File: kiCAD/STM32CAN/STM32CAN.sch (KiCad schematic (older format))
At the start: 25 parts, among them IC1 TPS560430X3FDBVR, J1 Conn_02x12_Odd_Even, J2 DB9_Male, J3 Conn_02x05_Odd_Even, U1 STM32F042F6Px, U2 TCAN332, Y1 Crystal

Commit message: Updated kiCAD drawing
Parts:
- removed D1: D_Schottky, symbol Device:D_Schottky
- removed IC1: TPS560430X3FDBVR, SOT95P280X145-6N, symbol SamacSys_Parts:TPS560430X3FDBVR
- removed L1: 6.8uH, symbol pspice:INDUCTOR
- removed R2: 51k, symbol Device:R
- removed R3: 22.1k, symbol Device:R
- added D1: PMEG6010CEJ, Diode_SMD:D_SOD-323, symbol Diode:PMEG6010CEJ
- added IC1: LMZM23601V3, SamacSys_Parts:LMZM23601V5SILR, symbol SamacSys_Parts:LMZM23601V3
- C1, C2, C3, C4, C5, C6, C7: footprint (none) -> Capacitor_SMD:C_0603_1608Metric
- C10: value 0.1uF -> 47uF; footprint (none) -> Capacitor_SMD:C_1206_3216Metric; Field4 (none) -> C3216X5R1E476M160AC
- C11: value 10uF -> 1uF; footprint (none) -> Capacitor_SMD:C_0603_1608Metric
- C8: value C -> 100nF; footprint (none) -> Capacitor_SMD:C_0603_1608Metric
- C9: value 2.2uF -> 10uF; footprint (none) -> Capacitor_SMD:C_0805_2012Metric; Field4 (none) -> C2012X5R1V106K085AC
- D2: footprint (none) -> Diode_SMD:D_0603_1608Metric
- J1: footprint (none) -> Connector_PinHeader_1.27mm:PinHeader_2x12_P1.27mm_Vertical_SMD
- J2: footprint (none) -> Connector_Dsub:DSUB-9_Male_Horizontal_P2.77x2.54mm_EdgePinOffset9.40mm
- J3: footprint (none) -> Connector_PinHeader_1.27mm:PinHeader_2x05_P1.27mm_Vertical_SMD
- R1: value R -> 470R; footprint (none) -> Resistor_SMD:R_0603_1608Metric
- R4: footprint (none) -> Resistor_SMD:R_0603_1608Metric
- U2: footprint (none) -> Package_SO:SOIC-8_3.9x4.9mm_P1.27mm
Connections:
- net GNDPWR is gone; now on net GNDREF: C11.2, C9.2, J2.6
- net +3V3: now also C10.1, IC1.6 (VOUT), IC1.7 (FB)
- net GNDREF: now also C10.2, IC1.1 (GND), IC1.11 (EP), IC1.2 (MODE/SYNC)
- net POWER_IN: now also D1.2 (A)
- net at C9.1: now also D1.1 (K), IC1.3 (VIN), IC1.4 (EN)
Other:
- moved on the sheet: C8

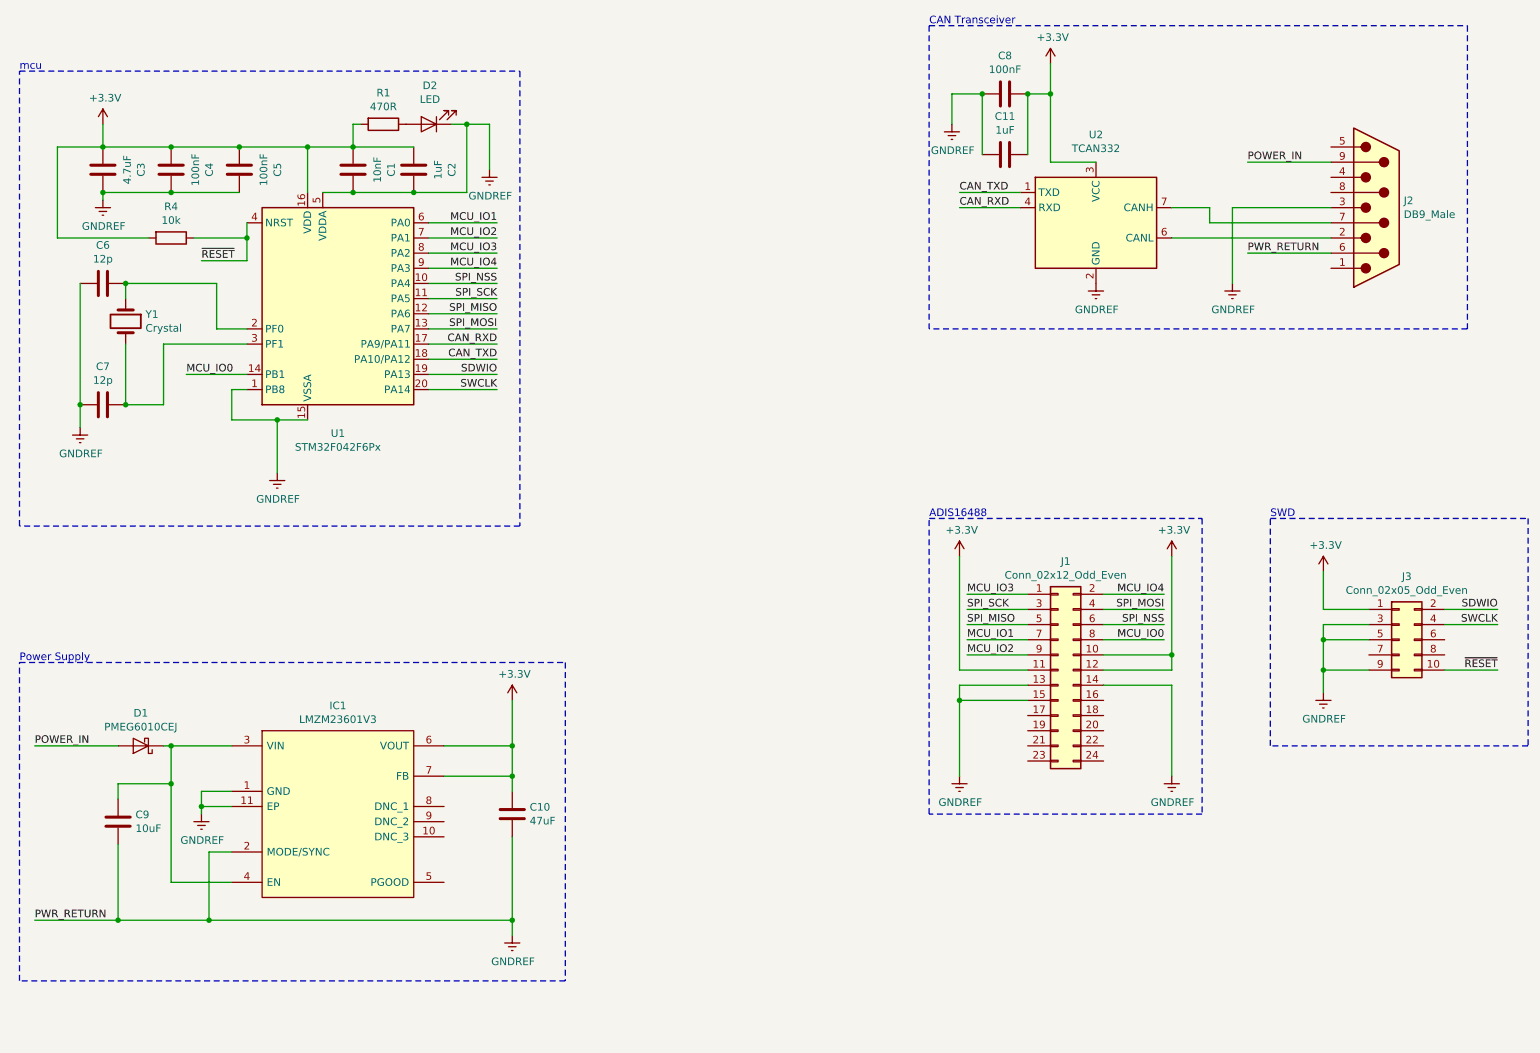
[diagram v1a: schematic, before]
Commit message: Started layout
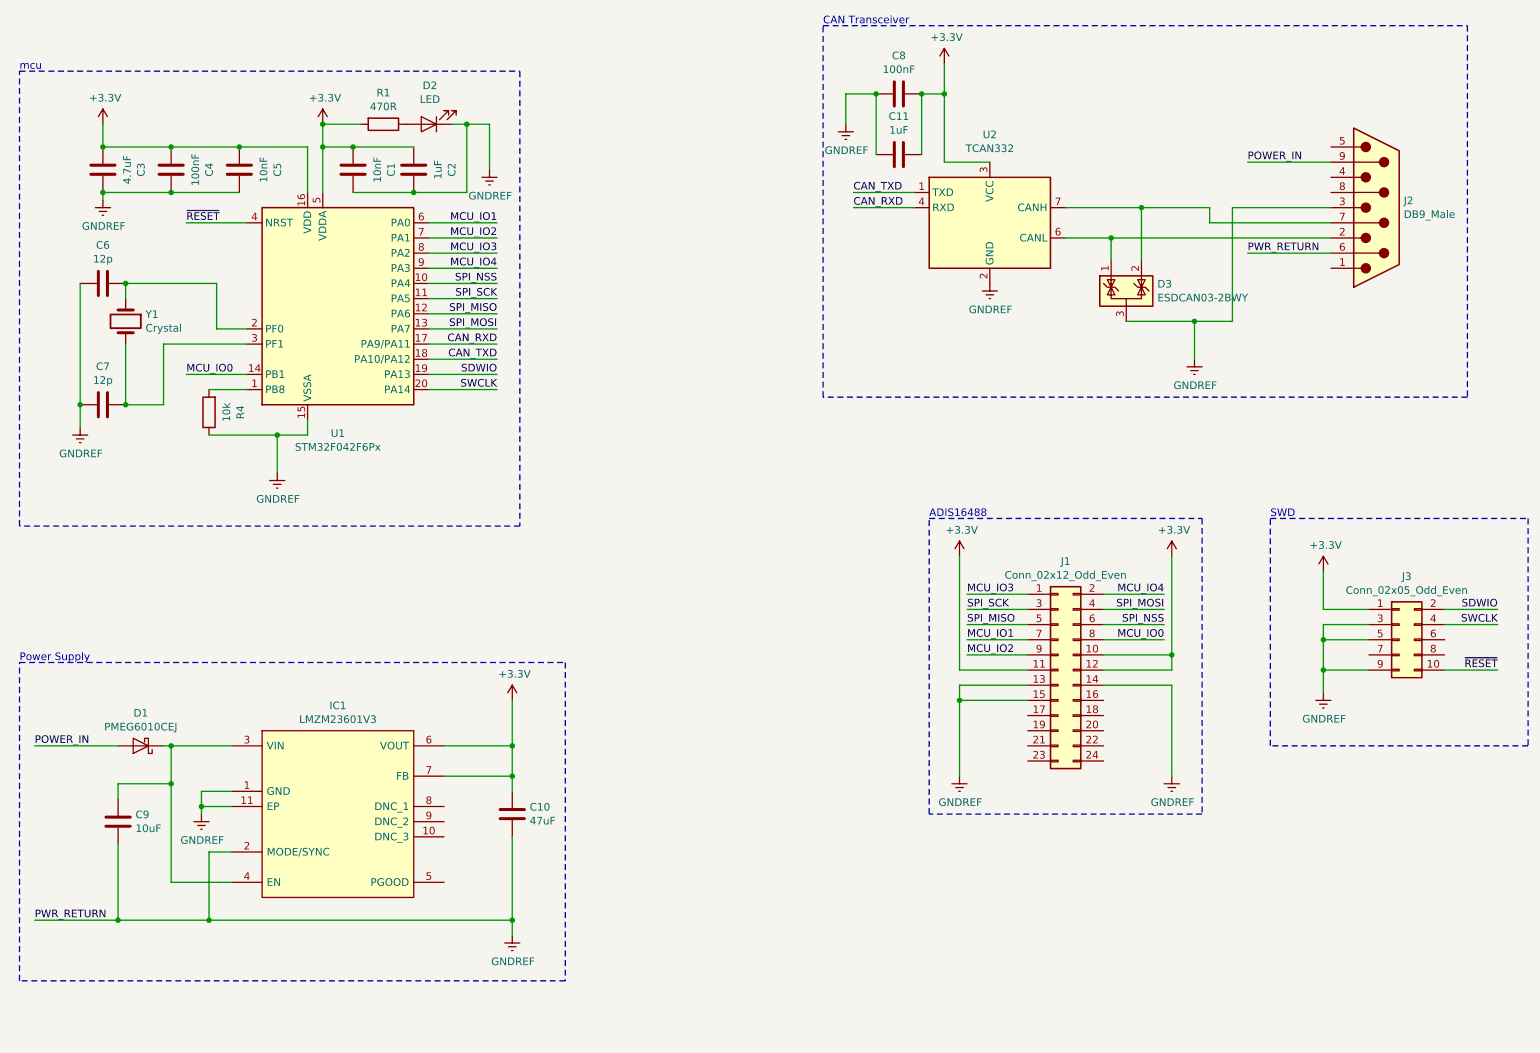
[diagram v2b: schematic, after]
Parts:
- added D3: ESDCAN03-2BWY, Package_TO_SOT_SMD:SOT-323_SC-70, symbol Power_Protection:NUP2105L
- C5: value 100nF -> 10nF
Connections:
- net +3V3: now also U1.5 (VDDA); no longer R4.2
- net GNDREF: now also R4.1, D3.3 (A); no longer U1.1 (PB8), U1.5 (VDDA)
- net ~RESET: no longer R4.1
- net at J2.2, U2.6 (CANL): now also D3.1 (K)
- net at J2.7, U2.7 (CANH): now also D3.2 (K)
- new net: R4.2, U1.1 (PB8)
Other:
- moved on the sheet: C11, C8, U2
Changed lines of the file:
@@
 	1    0    0    -1
 $EndComp
-Wire Wire Line
-	2500 3200 2400 3200
 $Comp
 L power:GNDREF #PWR0103
@@
 Text Label 4150 3200 2    50   ~ 0
 SWCLK
-Text Label 2200 2350 0    50   ~ 0
+Text Label 2100 2100 0    50   ~ 0
 ~RESET
 Text Label 4150 2500 2    50   ~ 0
@@
 	1    0    0    -1
 $EndComp
-Wire Wire Line
-	2900 3400 2700 3400
-Wire Wire Line
-	2700 3400 2700 3750
-Wire Wire Line
-	2400 3400 2700 3400
-Wire Wire Line
-	2400 3200 2400 3400
-Connection ~ 2700 3400
 $Comp
 L Device:C C5
@@
 P 2450 1750
 F 0 "C5" V 2198 1750 50  0000 C CNN
-F 1 "100nF" V 2289 1750 50  0000 C CNN
+F 1 "10nF" V 2289 1750 50  0000 C CNN
 F 2 "Capacitor_SMD:C_0603_1608Metric" H 2488 1600 50  0001 C CNN
 F 3 "~" H 2450 1750 50  0001 C CNN
@@
 	1    0    0    -1
 $EndComp
-Wire Wire Line
-	9000 2000 9000 2500
 $Comp
 L power:GNDREF #PWR0115
 U 1 1 5D0D2DBC
-P 9000 2500
-F 0 "#PWR0115" H 9000 2250 50  0001 C CNN
-F 1 "GNDREF" H 9005 2327 50  0000 C CNN
-F 2 "" H 9000 2500 50  0001 C CNN
-F 3 "" H 9000 2500 50  0001 C CNN
-	1    9000 2500
+P 8750 3000
+F 0 "#PWR0115" H 8750 2750 50  0001 C CNN
+F 1 "GNDREF" H 8755 2827 50  0000 C CNN
+F 2 "" H 8750 3000 50  0001 C CNN
+F 3 "" H 8750 3000 50  0001 C CNN
+	1    8750 3000
 	1    0    0    -1
 $EndComp
@@
 Text Label 9100 2300 0    50   ~ 0
 PWR_RETURN
-Wire Notes Line
-	10550 2800 7000 2800
 Wire Wire Line
 	9650 2100 8850 2100
 Wire Wire Line
 	8850 2100 8850 2000
-Wire Wire Line
-	8850 2000 8600 2000
-Wire Wire Line
-	9650 2200 8600 2200
 Wire Wire Line
 	9100 2300 9650 2300
@@
 	1    0    0    -1
 $EndComp
-Wire Wire Line
-	7800 1700 8100 1700
-Wire Wire Line
-	7200 2000 7600 2000
-Text Label 7200 2000 0    50   ~ 0
-CAN_RXD
-Wire Wire Line
-	7200 1900 7600 1900
-Text Label 7200 1900 0    50   ~ 0
-CAN_TXD
-$Comp
-L Interface_CAN_LIN:TCAN332 U2
-U 1 1 5D044387
-P 8100 2100
-F 0 "U2" H 8100 2681 50  0000 C CNN
-F 1 "TCAN332" H 8100 2590 50  0000 C CNN
-F 2 "Package_SO:SOIC-8_3.9x4.9mm_P1.27mm" H 8100 1600 50  0001 C CIN
-F 3 "http://www.ti.com/lit/ds/symlink/tcan337.pdf" H 8100 2100 50  0001 C CNN
-	1    8100 2100
-	1    0    0    -1
-$EndComp
 Text Notes 9250 4050 0    50   ~ 0
 SWD
@@
 	1    0    0    -1
 $EndComp
-$Comp
-L power:GNDREF #PWR0118
-U 1 1 5D05805C
-P 7150 1450
-F 0 "#PWR0118" H 7150 1200 50  0001 C CNN
-F 1 "GNDREF" H 7155 1277 50  0000 C CNN
-F 2 "" H 7150 1450 50  0001 C CNN
-F 3 "" H 7150 1450 50  0001 C CNN
-	1    7150 1450
-	1    0    0    -1
-$EndComp
-$Comp
-L Device:C C8
-U 1 1 5D0556B8
-P 7500 1250
-F 0 "C8" V 7248 1250 50  0000 C CNN
-F 1 "100nF" V 7339 1250 50  0000 C CNN
-F 2 "Capacitor_SMD:C_0603_1608Metric" H 7538 1100 50  0001 C CNN
-F 3 "~" H 7500 1250 50  0001 C CNN
-	1    7500 1250
-	0    1    1    0
-$EndComp
-$Comp
-L power:GNDREF #PWR0102
-U 1 1 5CFA5310
-P 8100 2500
-F 0 "#PWR0102" H 8100 2250 50  0001 C CNN
-F 1 "GNDREF" H 8105 2327 50  0000 C CNN
-F 2 "" H 8100 2500 50  0001 C CNN
-F 3 "" H 8100 2500 50  0001 C CNN
-	1    8100 2500
-	1    0    0    -1
-$EndComp
-$Comp
-L power:+3.3V #PWR0119
-U 1 1 5CFED302
-P 7800 1050
-F 0 "#PWR0119" H 7800 900 50  0001 C CNN
-F 1 "+3.3V" H 7815 1223 50  0000 C CNN
-F 2 "" H 7800 1050 50  0001 C CNN
-F 3 "" H 7800 1050 50  0001 C CNN
-	1    7800 1050
-	1    0    0    -1
-$EndComp
-Text Notes 7000 800  0    50   ~ 0
+Text Notes 6300 800  0    50   ~ 0
 CAN Transceiver
 $Comp
@@
 	1    0    0    -1
 $EndComp
-Connection ~ 2900 1600
 $Comp
 L Device:C C1
@@
 Connection ~ 3200 1600
 Wire Wire Line
-	3200 1600 2900 1600
-Wire Wire Line
-	3000 1900 3200 1900
-Connection ~ 3200 1900
-Wire Wire Line
 	3200 1900 3600 1900
 $Comp
@@
 Wire Wire Line
 	1950 2900 2500 2900
-$Comp
-L Device:R R4
-U 1 1 5D2B77E6
-P 2000 2200
-F 0 "R4" V 1793 2200 50  0000 C CNN
-F 1 "10k" V 1884 2200 50  0000 C CNN
-F 2 "Resistor_SMD:R_0603_1608Metric" V 1930 2200 50  0001 C CNN
-F 3 "~" H 2000 2200 50  0001 C CNN
-	1    2000 2200
-	0    1    1    0
-$EndComp
-Wire Wire Line
-	1250 1600 1550 1600
-Wire Wire Line
-	2500 2100 2500 2200
-Wire Wire Line
-	2150 2200 2500 2200
-Wire Wire Line
-	1850 2200 1250 2200
-Wire Wire Line
-	1250 1600 1250 2200
 Wire Wire Line
 	3850 1450 3950 1450
@@
 Wire Wire Line
 	3950 1450 4100 1450
-Wire Wire Line
-	3250 1450 3200 1450
-Wire Wire Line
-	3200 1450 3200 1600
 Wire Wire Line
 	1550 1900 1550 1950
@@
 Power Supply
 $Comp
+L Device:R R4
+U 1 1 5D05FAD3
+P 2250 3350
+F 0 "R4" V 2043 3350 50  0000 C CNN
+F 1 "10k" V 2134 3350 50  0000 C CNN
+F 2 "Resistor_SMD:R_0603_1608Metric" V 2180 3350 50  0001 C CNN
+F 3 "~" H 2250 3350 50  0001 C CNN
+	1    2250 3350
+	-1   0    0    1
+$EndComp
+Wire Wire Line
+	2250 3500 2700 3500
+Wire Wire Line
+	2900 3500 2900 3400
+Wire Wire Line
+	2700 3750 2700 3500
+Connection ~ 2700 3500
+Wire Wire Line
+	2700 3500 2900 3500
+Wire Wire Line
+	2250 3200 2500 3200
+Wire Wire Line
+	2500 2100 2100 2100
+Wire Wire Line
+	7100 1700 7400 1700
+Wire Wire Line
+	6500 2000 6900 2000
+Text Label 6500 2000 0    50   ~ 0
+CAN_RXD
+Wire Wire Line
+	6500 1900 6900 1900
+Text Label 6500 1900 0    50   ~ 0
+CAN_TXD
+$Comp
+L Interface_CAN_LIN:TCAN332 U2
+U 1 1 5D044387
+P 7400 2100
+F 0 "U2" H 7400 2681 50  0000 C CNN
+F 1 "TCAN332" H 7400 2590 50  0000 C CNN
+F 2 "Package_SO:SOIC-8_3.9x4.9mm_P1.27mm" H 7400 1600 50  0001 C CIN
+F 3 "http://www.ti.com/lit/ds/symlink/tcan337.pdf" H 7400 2100 50  0001 C CNN
+	1    7400 2100
+	1    0    0    -1
+$EndComp
+$Comp
+L power:GNDREF #PWR0118
+U 1 1 5D05805C
+P 6450 1450
+F 0 "#PWR0118" H 6450 1200 50  0001 C CNN
+F 1 "GNDREF" H 6455 1277 50  0000 C CNN
+F 2 "" H 6450 1450 50  0001 C CNN
+F 3 "" H 6450 1450 50  0001 C CNN
+	1    6450 1450
+	1    0    0    -1
+$EndComp
+$Comp
+L Device:C C8
+U 1 1 5D0556B8
+P 6800 1250
+F 0 "C8" V 6548 1250 50  0000 C CNN
+F 1 "100nF" V 6639 1250 50  0000 C CNN
+F 2 "Capacitor_SMD:C_0603_1608Metric" H 6838 1100 50  0001 C CNN
+F 3 "~" H 6800 1250 50  0001 C CNN
+	1    6800 1250
+	0    1    1    0
+$EndComp
+$Comp
+L power:GNDREF #PWR0102
+U 1 1 5CFA5310
+P 7400 2500
+F 0 "#PWR0102" H 7400 2250 50  0001 C CNN
+F 1 "GNDREF" H 7405 2327 50  0000 C CNN
+F 2 "" H 7400 2500 50  0001 C CNN
+F 3 "" H 7400 2500 50  0001 C CNN
+	1    7400 2500
+	1    0    0    -1
+$EndComp
+$Comp
+L power:+3.3V #PWR0119
+U 1 1 5CFED302
+P 7100 1050
+F 0 "#PWR0119" H 7100 900 50  0001 C CNN
+F 1 "+3.3V" H 7115 1223 50  0000 C CNN
+F 2 "" H 7100 1050 50  0001 C CNN
+F 3 "" H 7100 1050 50  0001 C CNN
+	1    7100 1050
+	1    0    0    -1
+$EndComp
+$Comp
 L Device:C C11
 U 1 1 5CFF2DCD
-P 7500 1650
-F 0 "C11" V 7248 1650 50  0000 C CNN
-F 1 "1uF" V 7339 1650 50  0000 C CNN
-F 2 "Capacitor_SMD:C_0603_1608Metric" H 7538 1500 50  0001 C CNN
-F 3 "~" H 7500 1650 50  0001 C CNN
-	1    7500 1650
+P 6800 1650
+F 0 "C11" V 6548 1650 50  0000 C CNN
+F 1 "1uF" V 6639 1650 50  0000 C CNN
+F 2 "Capacitor_SMD:C_0603_1608Metric" H 6838 1500 50  0001 C CNN
+F 3 "~" H 6800 1650 50  0001 C CNN
+	1    6800 1650
 	0    1    1    0
 $EndComp
 Wire Wire Line
-	7800 1050 7800 1250
-Wire Wire Line
-	7650 1650 7650 1250
-Wire Wire Line
-	7650 1250 7800 1250
-Connection ~ 7650 1250
-Connection ~ 7800 1250
-Wire Wire Line
-	7800 1250 7800 1700
-Wire Wire Line
-	7350 1250 7150 1250
-Wire Wire Line
-	7150 1450 7150 1250
-Wire Wire Line
-	7350 1650 7350 1250
-Connection ~ 7350 1250
-Wire Notes Line
-	7000 800  10550 800
-Wire Notes Line
-	7000 800  7000 2800
-Wire Notes Line
-	10550 800  10550 2800
-Wire Wire Line
-	2500 2200 2500 2350
-Wire Wire Line
-	2500 2350 2200 2350
-Connection ~ 2500 2200
+	7100 1050 7100 1250
+Wire Wire Line
+	6950 1650 6950 1250
+Wire Wire Line
+	6950 1250 7100 1250
+Connection ~ 6950 1250
+Connection ~ 7100 1250
+Wire Wire Line
+	7100 1250 7100 1700
+Wire Wire Line
+	6650 1250 6450 1250
+Wire Wire Line
+	6450 1450 6450 1250
+Wire Wire Line
+	6650 1650 6650 1250
+Connection ~ 6650 1250
+$Comp
+L Power_Protection:NUP2105L D3
+U 1 1 5D0995EE
+P 8300 2550
+F 0 "D3" H 8505 2596 50  0000 L CNN
+F 1 "ESDCAN03-2BWY " H 8505 2505 50  0000 L CNN
+F 2 "Package_TO_SOT_SMD:SOT-323_SC-70" H 8525 2500 50  0001 L CNN
+F 3 "https://no.mouser.com/datasheet/2/389/esdcan02-2bwy-954689.pdf" H 8425 2675 50  0001 C CNN
+	1    8300 2550
+	1    0    0    -1
+$EndComp
+Wire Wire Line
+	7900 2200 8200 2200
+Wire Wire Line
+	8200 2350 8200 2200
+Connection ~ 8200 2200
+Wire Wire Line
+	8200 2200 9650 2200
+Wire Wire Line
+	7900 2000 8400 2000
+Wire Wire Line
+	9000 2000 9000 2750
+Wire Wire Line
+	8400 2350 8400 2000
+Connection ~ 8400 2000
+Wire Wire Line
+	8400 2000 8850 2000
+Wire Notes Line
+	10550 3250 6300 3250
+Wire Notes Line
+	6300 3250 6300 800
+Wire Notes Line
+	6300 800  10550 800
+Wire Notes Line
+	10550 800  10550 3250
+Wire Wire Line
+	8300 2750 8750 2750
+Wire Wire Line
+	8750 3000 8750 2750
+Connection ~ 8750 2750
+Wire Wire Line
+	8750 2750 9000 2750
+Wire Wire Line
+	3000 1900 3000 1600
+Wire Wire Line
+	3000 1600 3200 1600
+$Comp
+L power:+3.3V #PWR?
+U 1 1 5D06C220
+P 3000 1450
+F 0 "#PWR?" H 3000 1300 50  0001 C CNN
+F 1 "+3.3V" H 3015 1623 50  0000 C CNN
+F 2 "" H 3000 1450 50  0001 C CNN
+F 3 "" H 3000 1450 50  0001 C CNN
+	1    3000 1450
+	1    0    0    -1
+$EndComp
+Wire Wire Line
+	3000 1450 3000 1600
+Connection ~ 3000 1600
+Wire Wire Line
+	3000 1450 3250 1450
+Connection ~ 3000 1450
 $EndSCHEMATC
